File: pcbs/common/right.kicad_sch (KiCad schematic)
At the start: 88 parts

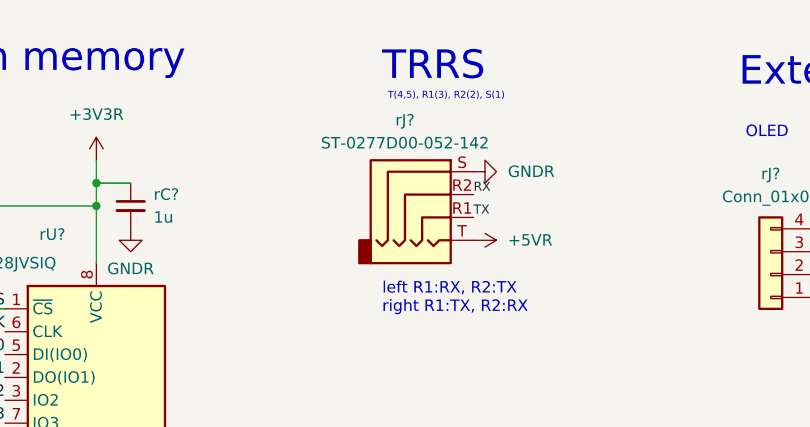
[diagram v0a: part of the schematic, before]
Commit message: Updated pcb for corne-chocolate to use PJ-606-6A audio jack
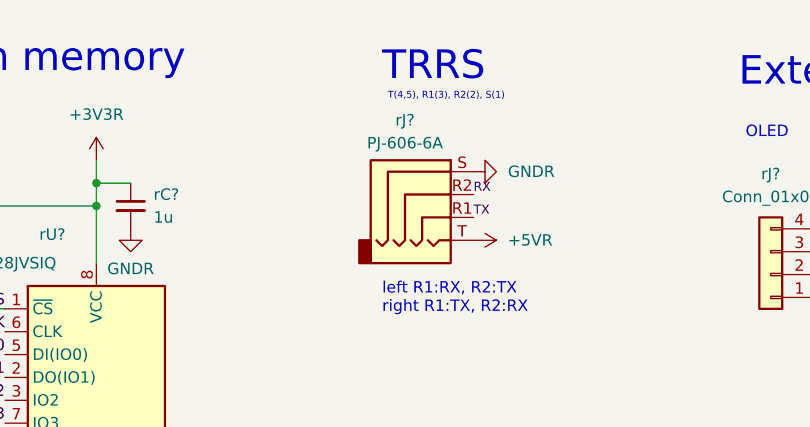
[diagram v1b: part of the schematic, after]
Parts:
- rEXLED? (x2), rLED? (x21): JLCPCB Part # (none) -> C5149201
- rEXSW? (x2): footprint kbd_local:keyswitch_cherrymx_hotswap_1u_rotary_encoder_ec12 -> kbd_local:keyswitch_choc12_hotswap_1u_rotary_encoder_ec12; JLCPCB Part # (none) -> C5333465
- rJ?: value ST-0277D00-052-142 -> PJ-606-6A; footprint kbd_local:ST-0277D00-052-142 -> kbd_local:PJ-606-6A; JLCPCB Part # C2837093 -> C145806
- rSW? (x20): footprint kbd:keyswitch_cherrymx_hotswap_1u -> kbd_local:keyswitch_choc12_hotswap_1u; JLCPCB Part # (none) -> C5333465
- rSW?: footprint kbd:keyswitch_cherrymx_hotswap_1.5u -> kbd_local:keyswitch_choc12_hotswap_1.5u; JLCPCB Part # (none) -> C5333465
